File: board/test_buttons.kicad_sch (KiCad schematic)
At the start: 10 parts, among them SW1 SW_Push, SW10 SW_Push, SW2 SW_Push, SW3 SW_Push, SW4 SW_SPDT, SW5 SW_Push, SW6 SW_Push, SW7 SW_Push, SW8 SW_Push, SW9 SW_Push

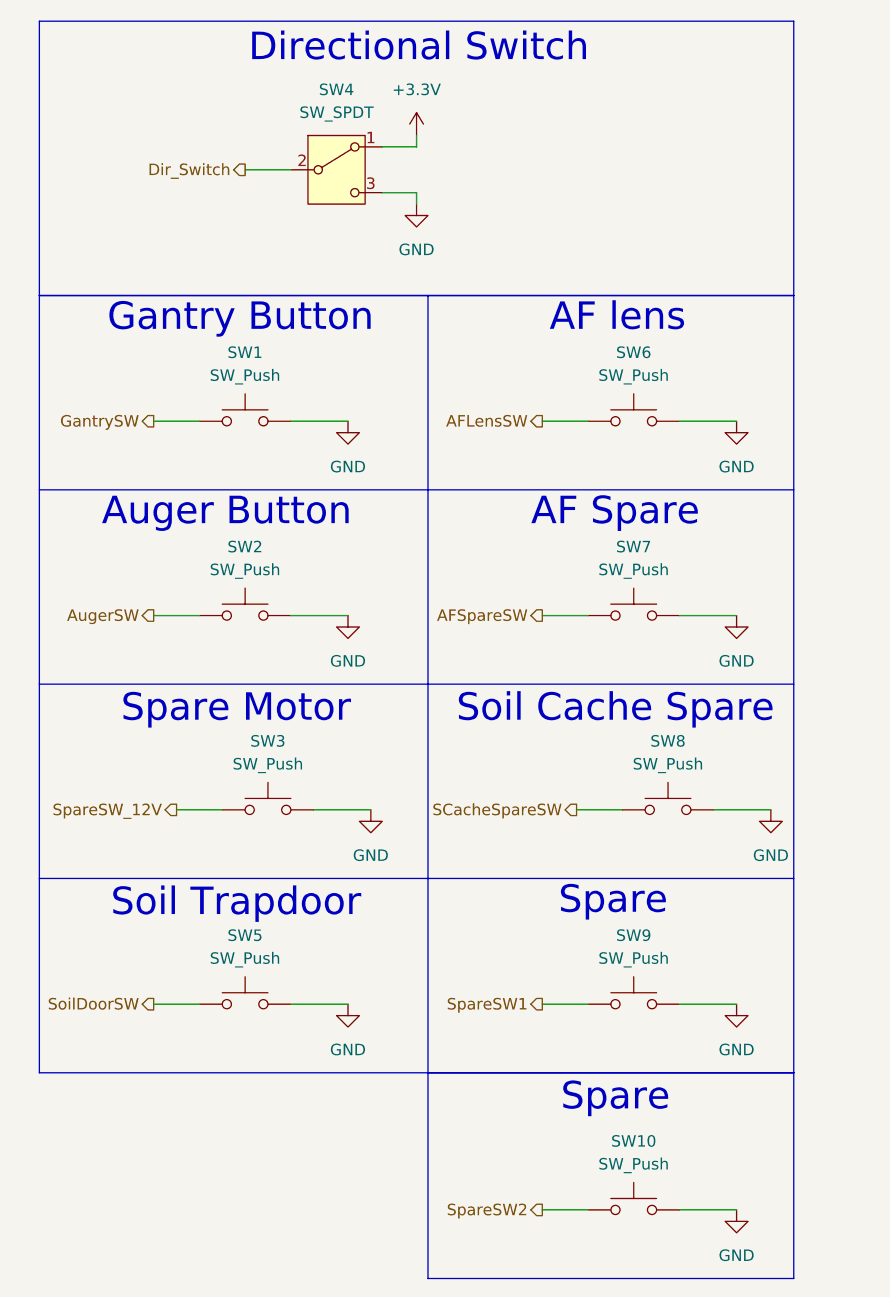
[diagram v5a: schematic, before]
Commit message: Layout Progress
Made a basic setup for locations, placed preliminary wires and text, rearranged teensy pins for simplicity
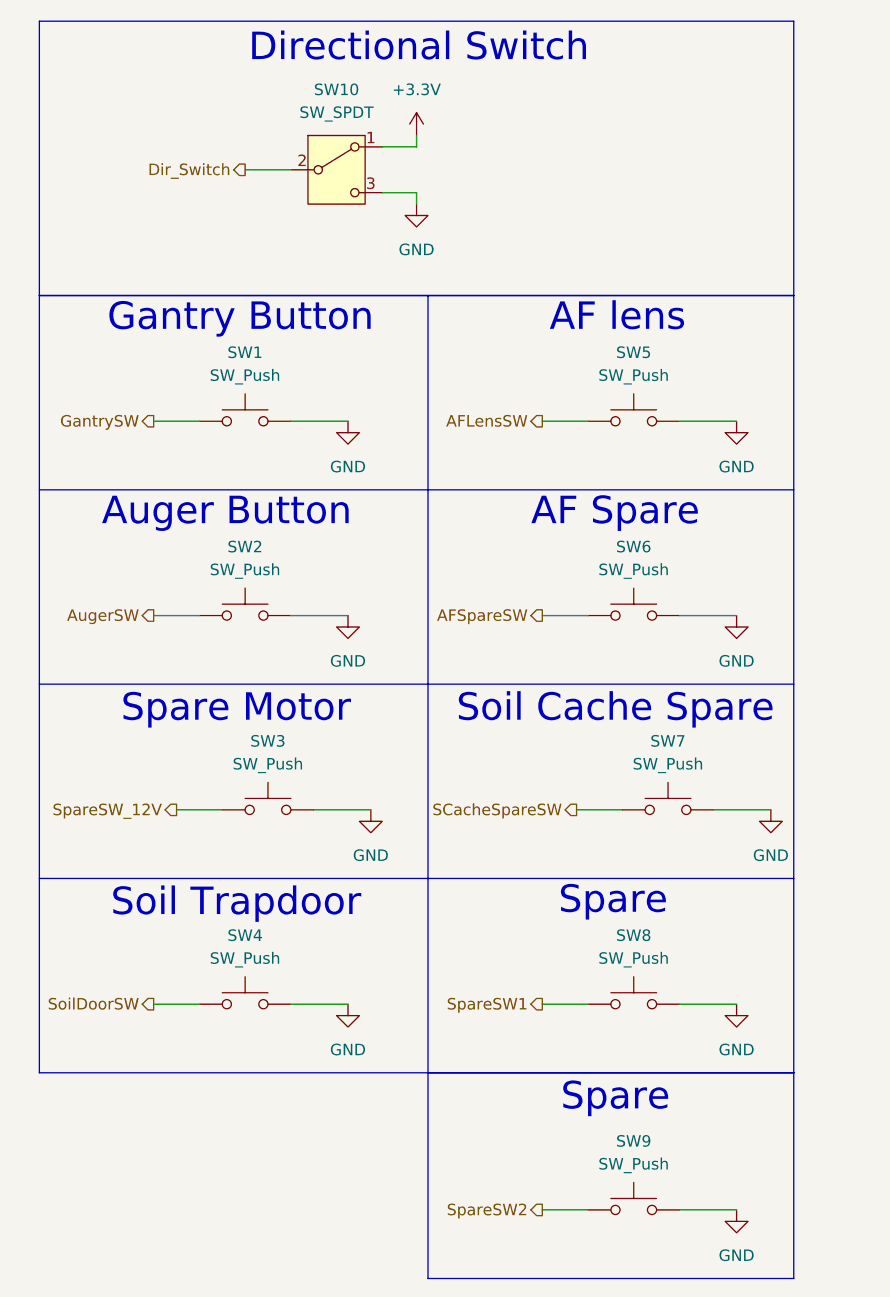
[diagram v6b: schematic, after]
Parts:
- renumbered SW4 to SW10, SW5 to SW4, SW6 to SW5, SW7 to SW6, SW8 to SW7, SW9 to SW8, SW10 to SW9
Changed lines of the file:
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@@
 		(dnp no)
 		(fields_autoplaced yes)
-		(property "Reference" "SW5"
+		(property "Reference" "SW4"
 			(at 35.56 114.3 0)
 			(effects
@@
 			(project "AugerBoard"
 				(path "/05fd3c2e-b986-4426-9c38-2a77d5c929de/590fcba9-6f33-46c6-897e-fddc0210fa05"
-					(reference "SW5")
+					(reference "SW4")
 					(unit 1)
 				)
@@
 		(on_board yes)
 		(dnp no)
-		(property "Reference" "SW6"
+		(property "Reference" "SW5"
 			(at 78.74 49.53 0)
 			(effects
@@
 			(project "AugerBoard"
 				(path "/05fd3c2e-b986-4426-9c38-2a77d5c929de/590fcba9-6f33-46c6-897e-fddc0210fa05"
-					(reference "SW6")
+					(reference "SW5")
 					(unit 1)
 				)
@@
 		(dnp no)
 		(fields_autoplaced yes)
-		(property "Reference" "SW10"
+		(property "Reference" "SW9"
 			(at 78.74 137.16 0)
 			(effects
@@
 			(project "AugerBoard"
 				(path "/05fd3c2e-b986-4426-9c38-2a77d5c929de/590fcba9-6f33-46c6-897e-fddc0210fa05"
-					(reference "SW10")
+					(reference "SW9")
 					(unit 1)
 				)
@@
 		(dnp no)
 		(fields_autoplaced yes)
-		(property "Reference" "SW9"
+		(property "Reference" "SW8"
 			(at 78.74 114.3 0)
 			(effects
@@
 			(project "AugerBoard"
 				(path "/05fd3c2e-b986-4426-9c38-2a77d5c929de/590fcba9-6f33-46c6-897e-fddc0210fa05"
-					(reference "SW9")
+					(reference "SW8")
 					(unit 1)
 				)
@@
 		(dnp no)
 		(fields_autoplaced yes)
-		(property "Reference" "SW4"
+		(property "Reference" "SW10"
 			(at 45.72 20.32 0)
 			(effects
@@
 			(project ""
 				(path "/05fd3c2e-b986-4426-9c38-2a77d5c929de/590fcba9-6f33-46c6-897e-fddc0210fa05"
-					(reference "SW4")
+					(reference "SW10")
 					(unit 1)
 				)
@@
 		(dnp no)
 		(fields_autoplaced yes)
-		(property "Reference" "SW7"
+		(property "Reference" "SW6"
 			(at 78.74 71.12 0)
 			(effects
@@
 			(project "AugerBoard"
 				(path "/05fd3c2e-b986-4426-9c38-2a77d5c929de/590fcba9-6f33-46c6-897e-fddc0210fa05"
-					(reference "SW7")
+					(reference "SW6")
 					(unit 1)
 				)
@@
 		(dnp no)
 		(fields_autoplaced yes)
-		(property "Reference" "SW8"
+		(property "Reference" "SW7"
 			(at 82.55 92.71 0)
 			(effects
@@
 			(project "AugerBoard"
 				(path "/05fd3c2e-b986-4426-9c38-2a77d5c929de/590fcba9-6f33-46c6-897e-fddc0210fa05"
-					(reference "SW8")
-					(unit 1)
-				)
+					(reference "SW7")
+					(unit 1)
+				)

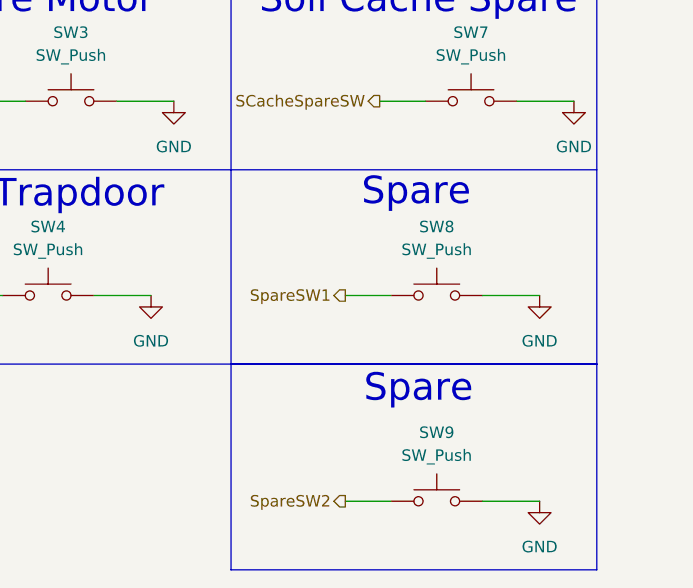
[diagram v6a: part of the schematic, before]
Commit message: added pin for AF, added gimbal names, refined look
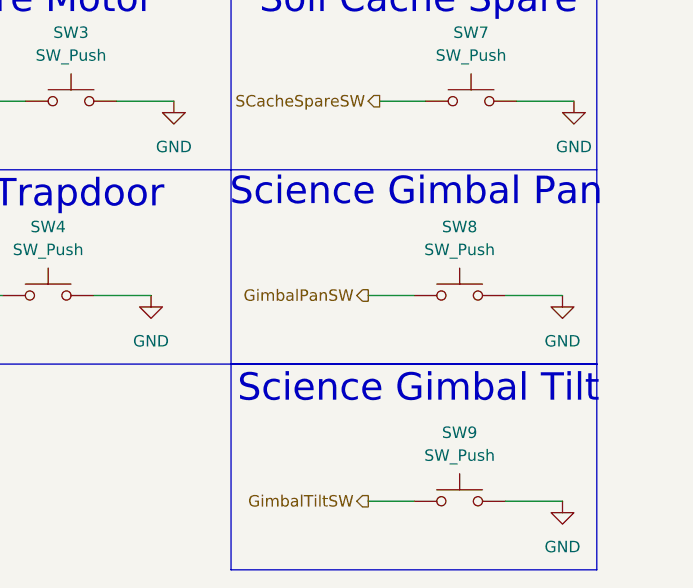
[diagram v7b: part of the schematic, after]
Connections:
- net SpareSW1 renamed GimbalPanSW
- net SpareSW2 renamed GimbalTiltSW
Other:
- note added: "Science Gimbal Pan"
- note added: "Science Gimbal Tilt"
- note removed: "Spare"
- moved on the sheet: SW8, SW9
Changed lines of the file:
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@@
 		)
 	)
-	(text "Spare"
+	(text "Science Gimbal Pan"
 		(exclude_from_sim no)
 		(at 76.454 110.49 0)
@@
 		)
 	)
-	(text "Spare"
+	(text "Science Gimbal Tilt"
 		(exclude_from_sim no)
 		(at 76.708 132.334 0)
@@
 	(wire
 		(pts
-			(xy 68.58 144.78) (xy 73.66 144.78)
+			(xy 71.12 144.78) (xy 76.2 144.78)
 		)
 		(stroke
@@
 	(wire
 		(pts
-			(xy 83.82 121.92) (xy 90.17 121.92)
+			(xy 86.36 121.92) (xy 92.71 121.92)
 		)
 		(stroke
@@
 	(wire
 		(pts
-			(xy 83.82 144.78) (xy 90.17 144.78)
+			(xy 86.36 144.78) (xy 92.71 144.78)
 		)
 		(stroke
@@
 	(wire
 		(pts
-			(xy 68.58 121.92) (xy 73.66 121.92)
-		)
-		(stroke
-			(width 0)
-			(type default)
-		)
-	)
-	(hierarchical_label "SpareSW1"
+			(xy 71.12 121.92) (xy 76.2 121.92)
+		)
+		(stroke
+			(width 0)
+			(type default)
+		)
+	)
+	(hierarchical_label "GimbalPanSW"
 		(shape output)
-		(at 68.58 121.92 180)
+		(at 71.12 121.92 180)
 		(effects
 			(font
@@
 		)
 	)
-	(hierarchical_label "SpareSW2"
+	(hierarchical_label "GimbalTiltSW"
 		(shape output)
-		(at 68.58 144.78 180)
+		(at 71.12 144.78 180)
 		(effects
 			(font
@@
 	(symbol
 		(lib_id "power:GND")
-		(at 90.17 144.78 0)
+		(at 92.71 144.78 0)
 		(unit 1)
 		(exclude_from_sim no)
@@
 		(fields_autoplaced yes)
 		(property "Reference" "#PWR063"
-			(at 90.17 151.13 0)
+			(at 92.71 151.13 0)
 			(effects
 				(font
@@
 		)
 		(property "Value" "GND"
-			(at 90.17 149.86 0)
+			(at 92.71 149.86 0)
 			(effects
 				(font
@@
 		)
 		(property "Footprint" ""
-			(at 90.17 144.78 0)
+			(at 92.71 144.78 0)
 			(effects
 				(font
@@
 		)
 		(property "Datasheet" ""
-			(at 90.17 144.78 0)
+			(at 92.71 144.78 0)
 			(effects
 				(font
@@
 		)
 		(property "Description" "Power symbol creates a global label with name \"GND\" , ground"
-			(at 90.17 144.78 0)
+			(at 92.71 144.78 0)
 			(effects
 				(font
@@
 	(symbol
 		(lib_id "Switch:SW_Push")
-		(at 78.74 144.78 0)
+		(at 81.28 144.78 0)
 		(unit 1)
 		(exclude_from_sim no)
@@
 		(fields_autoplaced yes)
 		(property "Reference" "SW9"
-			(at 78.74 137.16 0)
+			(at 81.28 137.16 0)
 			(effects
 				(font
@@
 		)
 		(property "Value" "SW_Push"
-			(at 78.74 139.7 0)
+			(at 81.28 139.7 0)
 			(effects
 				(font
@@
 		)
 		(property "Footprint" "Button_Switch_SMD:SW_SPST_TL3305A"
-			(at 78.74 139.7 0)
+			(at 81.28 139.7 0)
 			(effects
 				(font
@@
 		)
 		(property "Datasheet" "~"
-			(at 78.74 139.7 0)
+			(at 81.28 139.7 0)
 			(effects
 				(font
@@
 		)
 		(property "Description" "Push button switch, generic, two pins"
-			(at 78.74 144.78 0)
+			(at 81.28 144.78 0)
 			(effects
 				(font
@@
 	(symbol
 		(lib_id "Switch:SW_Push")
-		(at 78.74 121.92 0)
+		(at 81.28 121.92 0)
 		(unit 1)
 		(exclude_from_sim no)
@@
 		(fields_autoplaced yes)
 		(property "Reference" "SW8"
-			(at 78.74 114.3 0)
+			(at 81.28 114.3 0)
 			(effects
 				(font
@@
 		)
 		(property "Value" "SW_Push"
-			(at 78.74 116.84 0)
+			(at 81.28 116.84 0)
 			(effects
 				(font
@@
 		)
 		(property "Footprint" "Button_Switch_SMD:SW_SPST_TL3305A"
-			(at 78.74 116.84 0)
+			(at 81.28 116.84 0)
 			(effects
 				(font
@@
 		)
 		(property "Datasheet" "~"
-			(at 78.74 116.84 0)
+			(at 81.28 116.84 0)
 			(effects
 				(font
@@
 		)
 		(property "Description" "Push button switch, generic, two pins"
-			(at 78.74 121.92 0)
+			(at 81.28 121.92 0)
 			(effects
 				(font
@@
 	(symbol
 		(lib_id "power:GND")
-		(at 90.17 121.92 0)
+		(at 92.71 121.92 0)
 		(unit 1)
 		(exclude_from_sim no)
@@
 		(fields_autoplaced yes)
 		(property "Reference" "#PWR062"
-			(at 90.17 128.27 0)
+			(at 92.71 128.27 0)
 			(effects
 				(font
@@
 		)
 		(property "Value" "GND"
-			(at 90.17 127 0)
+			(at 92.71 127 0)
 			(effects
 				(font
@@
 		)
 		(property "Footprint" ""
-			(at 90.17 121.92 0)
+			(at 92.71 121.92 0)
 			(effects
 				(font
@@
 		)
 		(property "Datasheet" ""
-			(at 90.17 121.92 0)
+			(at 92.71 121.92 0)
 			(effects
 				(font
@@
 		)
 		(property "Description" "Power symbol creates a global label with name \"GND\" , ground"
-			(at 90.17 121.92 0)
-			(effects
-				(font
+			(at 92.71 121.92 0)
+			(effects
+				(font

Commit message: Redesigning Layout
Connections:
- net AFSpareSW renamed SpareSW1
- net SCacheSpareSW renamed SpareSW2
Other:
- note added: "Spare 1"
- note added: "Spare 12V"
- note added: "Spare 2"
- note removed: "AF Spare"
- note removed: "Soil Cache Spare"
- note removed: "Spare Motor"
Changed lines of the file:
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@@
 		)
 	)
-	(text "Soil Cache Spare"
+	(text "Spare 2"
 		(exclude_from_sim no)
 		(at 76.708 89.154 0)
@@
 		)
 	)
-	(text "AF Spare"
+	(text "Spare 1"
 		(exclude_from_sim no)
 		(at 76.708 67.31 0)
@@
 		)
 	)
-	(text "Spare Motor"
+	(text "Spare 12V"
 		(exclude_from_sim no)
 		(at 34.544 89.154 0)
@@
 		)
 	)
-	(hierarchical_label "SCacheSpareSW"
+	(hierarchical_label "SpareSW2"
 		(shape output)
 		(at 72.39 100.33 180)
@@
 		)
 	)
-	(hierarchical_label "AFSpareSW"
+	(hierarchical_label "SpareSW1"
 		(shape output)
 		(at 68.58 78.74 180)
